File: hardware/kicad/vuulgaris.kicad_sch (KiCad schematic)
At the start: 309 parts, among them J1 TFPUSH, J10 PJ-603_C41409498, J11 TYPE-C-31-M-12, J12 FACEPLATE 2x5 IDC, J2 PJ-376, J3 PJ-376, J4 PJ-376, J5 PJ-376, J6 PJ-376, J7 PJ-603_C41409498, J8 PJ-603_C41409498, J9 PJ-603_C41409498, Q1 J113 / MMBFJ113, Q2 J113 / MMBFJ113, SW1 SW_DPDT_FLAT, SW2 SW_DPDT_FLAT, SW4 12x12 tactile, SW5 12x12 tactile, SW6 12x12 tactile, SW7 12x12 tactile, SW8 12x12 tactile, SW9 12x12 tactile, U1 ES_DAISY_PATCH_SM_REV1, U10 OPA1688_FLAT, U101 V3205SD, U102 TL072_FLAT, U103 TL072_FLAT, U104 CD4046B, U106 TL072_FLAT, U201 V3205SD, U202 TL072_FLAT, U203 TL072_FLAT, U204 CD4046B, U206 TL072_FLAT, U3 MCP23017-E_SO, U301 TL084, U302 TL074, U4 MCP23017-E_SO, U401 TL084, U402 TL074, U5 AMS1117-3.3, U6 AMS1117-3.3, U7 DKM10E-12, U8 AMS1117-5.0, U9 OPA1688_FLAT

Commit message: hardware: fix the LPG LED drive -- it was built inverted
Bergman's drawing runs the two vactrol LEDs between the clamp node and the
op-amp output: anodes on the node with R17 and D1, cathodes returning
through R6 470R to U1-B pin 7. The LED string never touches ground. U1-B
swings negative, the node sits at -3.9V where D1 is in reverse breakdown,
and D1 is what supplies the LED current.

We built the mirror image: R6 feeding the anode node, both cathodes to
ground, and the zener turned around. With our op-amp still swinging
negative -- OFFSET sits on +12V into an inverting stage -- the flipped
zener pins the node at -0.7V and the LEDs never light. Where the real
circuit has the zener supplying LED current, ours shunts it away above
3.9V. The core of the instrument would not have opened.

Per channel: D301/D401 turned around (rotated 180 so the existing copper
still lands correctly), VT302.2/VT402.2 moved off GND onto the new
LPG_LEDK_L/_R, and R306/R406 moved to sit between the LED cathodes and the
op-amp output. R417 kept its path to the node, which used to run through
R406's pad. The In2 ground plane was refilled so it clears the two pads
that left GND -- without that the pour would have shorted them.

0 unconnected, 0 clearance violations, 942/942 parity. Fab outputs
regenerated.
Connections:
- net GND: now also D301.1 (C), D401.1 (C); no longer D301.2 (A), D401.2 (A), VT302.2 (K), VT402.2 (K)
- net LPG_LED_L: now also D301.2 (A); no longer D301.1 (C), R306.2
- net LPG_LED_R: now also D401.2 (A); no longer D401.1 (C), R406.2
- new net LPG_LEDK_L: R306.2, VT302.2 (K)
- new net LPG_LEDK_R: R406.2, VT402.2 (K)
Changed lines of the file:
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@@
     (effects (font (size 1.27 1.27)) (justify left bottom))
   )
-  (label "LPG_LED_L" (at 104.76 3900.0 180) (fields_autoplaced)
-    (effects (font (size 1.27 1.27)) (justify left bottom))
-  )
-  (label "GND" (at 135.24 3900.0 0) (fields_autoplaced)
-    (effects (font (size 1.27 1.27)) (justify left bottom))
-  )
-  (label "LPG_LED_R" (at 304.76 3900.0 180) (fields_autoplaced)
-    (effects (font (size 1.27 1.27)) (justify left bottom))
-  )
-  (label "GND" (at 335.24 3900.0 0) (fields_autoplaced)
+  (label "GND" (at 104.76 3900.0 180) (fields_autoplaced)
+    (effects (font (size 1.27 1.27)) (justify left bottom))
+  )
+  (label "LPG_LED_L" (at 135.24 3900.0 0) (fields_autoplaced)
+    (effects (font (size 1.27 1.27)) (justify left bottom))
+  )
+  (label "GND" (at 304.76 3900.0 180) (fields_autoplaced)
+    (effects (font (size 1.27 1.27)) (justify left bottom))
+  )
+  (label "LPG_LED_R" (at 335.24 3900.0 0) (fields_autoplaced)
     (effects (font (size 1.27 1.27)) (justify left bottom))
   )
@@
     (effects (font (size 1.27 1.27)) (justify left bottom))
   )
-  (label "LPG_LED_L" (at 510.0 3103.97 270) (fields_autoplaced)
+  (label "LPG_LEDK_L" (at 510.0 3103.97 270) (fields_autoplaced)
     (effects (font (size 1.27 1.27)) (justify left bottom))
   )
@@
     (effects (font (size 1.27 1.27)) (justify left bottom))
   )
-  (label "LPG_LED_R" (at 510.0 3403.97 270) (fields_autoplaced)
+  (label "LPG_LEDK_R" (at 510.0 3403.97 270) (fields_autoplaced)
     (effects (font (size 1.27 1.27)) (justify left bottom))
   )
@@
     (effects (font (size 1.27 1.27)) (justify left bottom))
   )
-  (label "GND" (at 697.14 4022.54 180) (fields_autoplaced)
+  (label "LPG_LEDK_L" (at 697.14 4022.54 180) (fields_autoplaced)
     (effects (font (size 1.27 1.27)) (justify left bottom))
   )
@@
     (effects (font (size 1.27 1.27)) (justify left bottom))
   )
-  (label "GND" (at 1097.14 4022.54 180) (fields_autoplaced)
-    (effects (font (size 1.27 1.27)) (justify left bottom))
-  )
+  (label "LPG_LEDK_R" (at 1097.14 4022.54 180) (fields_autoplaced)
+    (effects (font (size 1.27 1.27)) (justify left bottom))
+  )

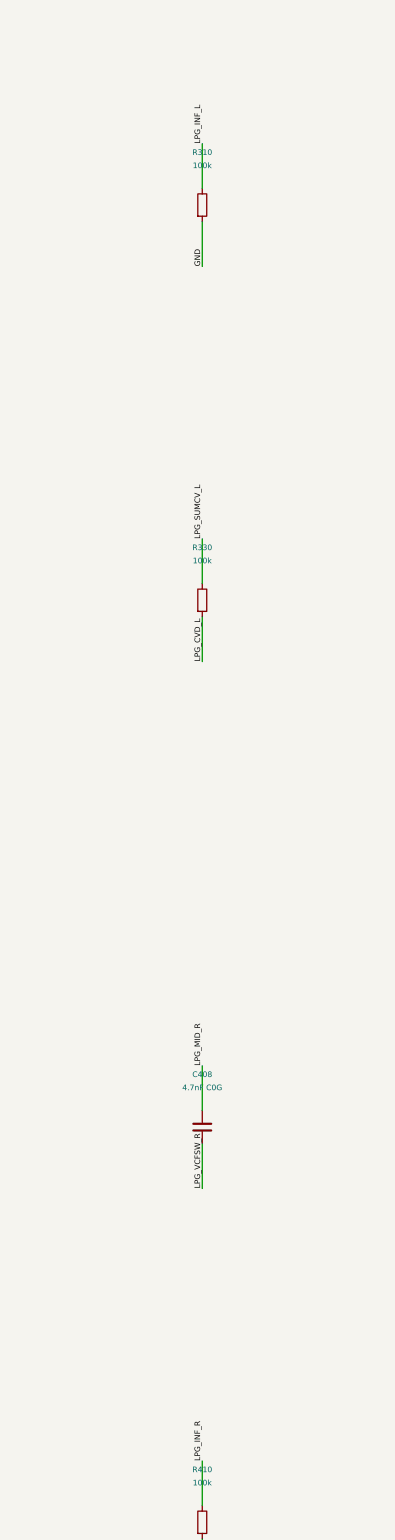
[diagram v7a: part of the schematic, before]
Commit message: hardware: R9 belongs before the input cap, not after it
Bergman puts R9 100K on the jack side of C6 and R10 100K after it. We had
both after, which is 50k of bias on the op-amp input instead of 100k, and
nothing at all loading the source side.

R310/R410 move to the pre-cap node, so on this board R310 is Bergman's R9
and R309 is R10. One trace deleted and a short jog to the existing
AUDIO_OUT run per channel; the L jog sits at y=118.9 to clear a B.Cu
P3V3_DAISY run underneath. Plane refilled, fab regenerated.

Caught by eye off the drawing, like the LED drive. The "checked against
the drawing" table in lpg-bergman.md vouched for this too.

0 unconnected, 0 clearance violations, 942/942 parity.
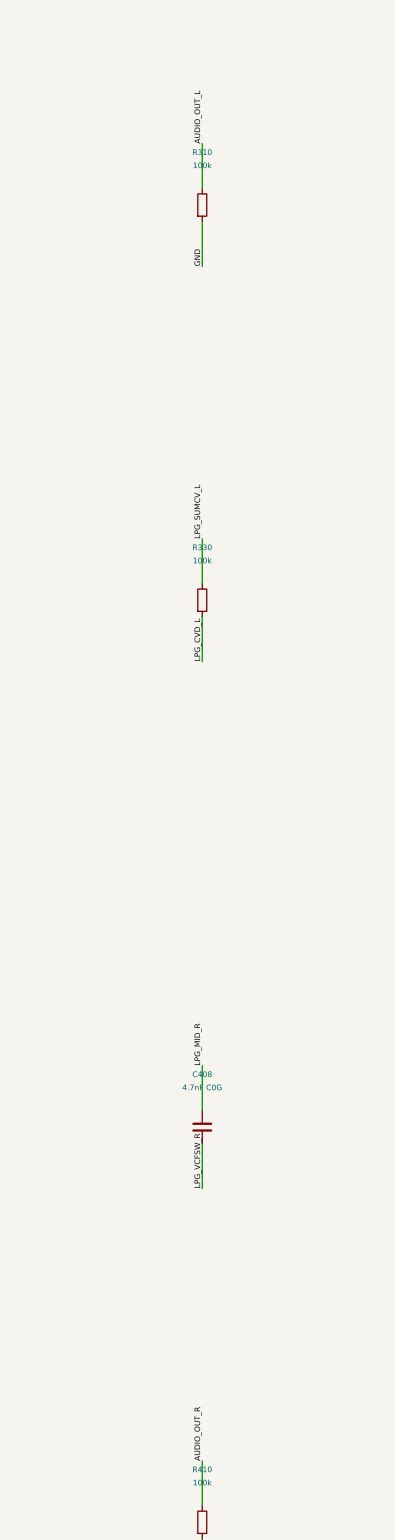
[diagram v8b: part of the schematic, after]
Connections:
- net AUDIO_OUT_L: now also R310.1
- net AUDIO_OUT_R: now also R410.1
- net LPG_INF_L: no longer R310.1
- net LPG_INF_R: no longer R410.1
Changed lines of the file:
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@@
     (effects (font (size 1.27 1.27)) (justify left bottom))
   )
-  (label "LPG_INF_L" (at 1030.0 3076.03 90) (fields_autoplaced)
+  (label "AUDIO_OUT_L" (at 1030.0 3076.03 90) (fields_autoplaced)
     (effects (font (size 1.27 1.27)) (justify left bottom))
   )
@@
     (effects (font (size 1.27 1.27)) (justify left bottom))
   )
-  (label "LPG_INF_R" (at 1030.0 3376.03 90) (fields_autoplaced)
+  (label "AUDIO_OUT_R" (at 1030.0 3376.03 90) (fields_autoplaced)
     (effects (font (size 1.27 1.27)) (justify left bottom))
   )
